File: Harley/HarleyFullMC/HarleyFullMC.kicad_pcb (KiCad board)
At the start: 10 copper layers, 33 x 45 mm, 209 parts, among them J1 USB_3.1_microB, J3 CONN_01X04, J4 CONN_02X05, J5 DF40C_60DP_0-4V, J6 CONN_01X06, U1 xc7a50tcsg324pkg, U10 LTM4622, U11 OSCILLATOR, U12 24LC128T-I/MNY, U2 LTM4622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

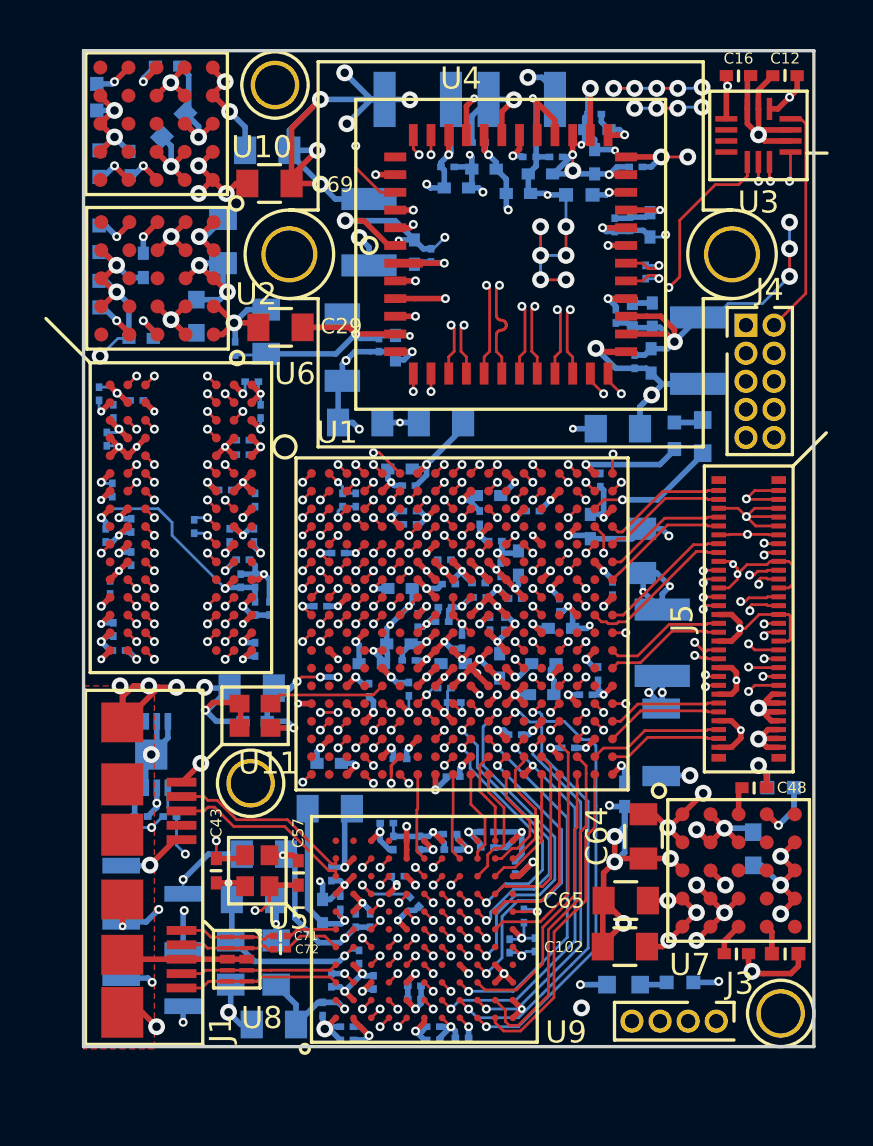
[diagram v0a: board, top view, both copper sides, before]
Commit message: fixed things based on Harley Notes, not ready for fab yet
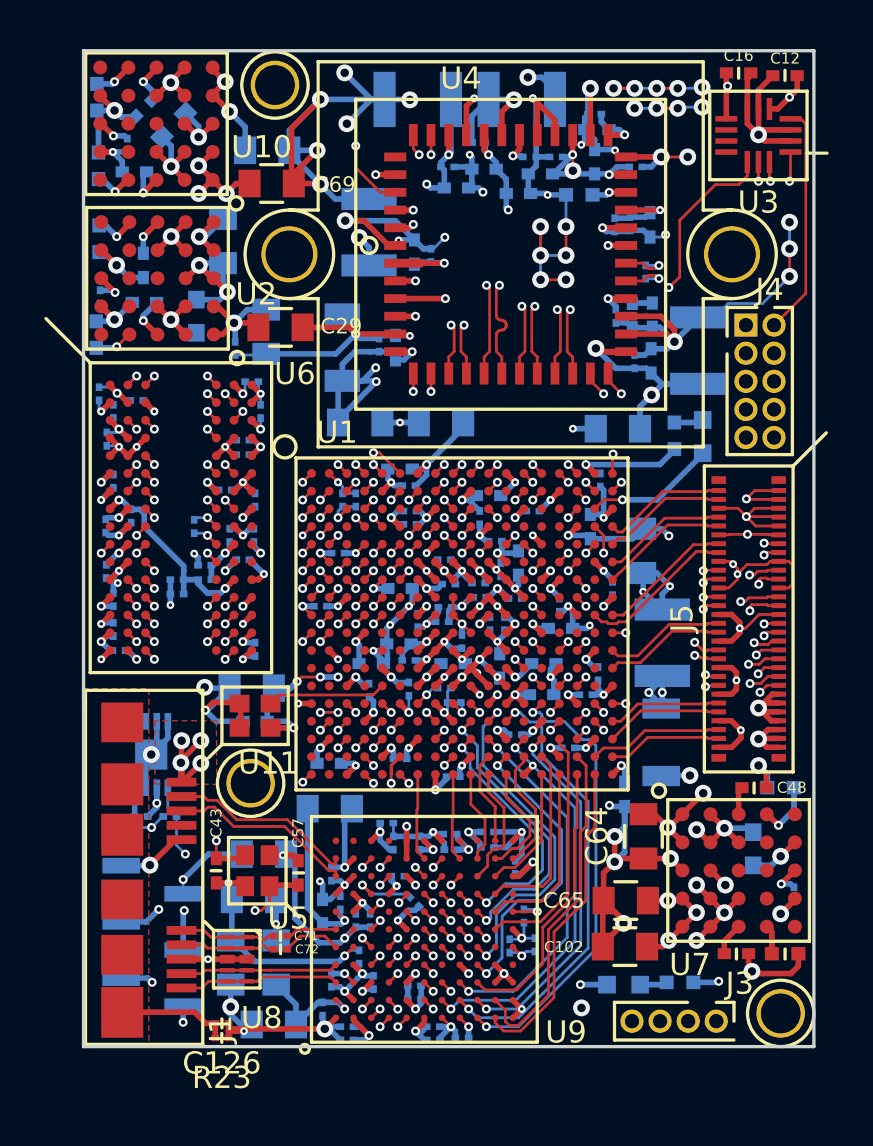
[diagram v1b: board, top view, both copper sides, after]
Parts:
- added C126: 4.7n, Dipoles_SMD:C_0201, F.Cu at (18.2, 196.9)
- added R23: 1M, Dipoles_SMD:C_0201, F.Cu at (18.2, 197.6)
- added R24: R, Dipoles_SMD:C_0201, B.Cu at (44.1, 191.1)
- added R25: R, Dipoles_SMD:C_0201, B.Cu at (12.8, 164.1)
- added R26: R, Dipoles_SMD:C_0201, B.Cu at (14.0, 157.3)
- moved R7 3.53 mm to (16.2, 176.9), turned to 180 degrees
- moved C49 3.52 mm to (17.5, 176.2), turned to 180 degrees
- moved C26 2.94 mm to (16.2, 177.6), turned to 180 degrees
- moved R6 2.62 mm to (17.5, 176.9), turned to 180 degrees
- moved C66 2.18 mm to (14.7, 155.6), turned to 225 degrees
- moved R8 1.83 mm to (12.6, 165.8)
- moved C3 1.63 mm to (14.8, 164.4)
- moved C23 1.45 mm to (14.2, 174.0)
- moved C45 1.26 mm to (13.0, 176.5)
- moved C60 1.15 mm to (13.0, 174.5)
- moved C50 0.57 mm to (13.3, 177.8)
- moved C68 0.43 mm to (14.3, 158.5), turned to 180 degrees
- moved C51 0.40 mm to (13.3, 172.4)
- moved C16 0.12 mm to (41.6, 154.0)
- moved R5 0.10 mm to (12.7, 158.2)
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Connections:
- J1 pad SHLD: GND -> Net-(C126-Pad1)
- J5 pad 36: GND -> FPGA_SS_CCLK
- J5 pad 38: FPGA_SS_CCLK -> FPGA_SS_DIN
- U10 pad C5: GND -> Net-(R26-Pad1)
- U12 pad EPAD: (no net) -> GND
- U2 pad C5: GND -> Net-(R25-Pad1)
- U7 pad C5: GND -> Net-(R24-Pad1)
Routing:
- net GND: track 405.8 -> 387.6 mm, vias 211 -> 208
- net FPGA_SS_DIN: track 32.6 -> 40.0 mm, vias 2 -> 3
- net +1V8: track 41.7 -> 35.8 mm
- net Net-(C126-Pad1): track 0.00 -> 5.07 mm
- net +5V: track 33.2 -> 38.2 mm, vias 13 -> 16
- net DDR_VREF: track 11.7 -> 9.29 mm
- net Net-(R25-Pad1): track 0.00 -> 1.62 mm, vias 0 -> 1
- net Net-(R24-Pad1): track 0.00 -> 1.50 mm, vias 0 -> 1
- net Net-(R26-Pad1): track 0.00 -> 1.50 mm, vias 0 -> 1
- net DDR_CAS#: track 8.62 -> 9.42 mm
- net (no net): track 0.00 -> 0.80 mm, vias 1 -> 3
- net DDR_RAS#: track 9.29 -> 10.1 mm
- net DDR_VDD: track 47.8 -> 48.5 mm
- net FPGA_SS_CCLK: track 44.7 -> 44.2 mm
- added copper zone on F.Cu, net +5V
- added copper zone on F.Cu, net Net-(C126-Pad1)
- removed copper zone on F.Cu, net GND

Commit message: fixed footprints and rerouted imager
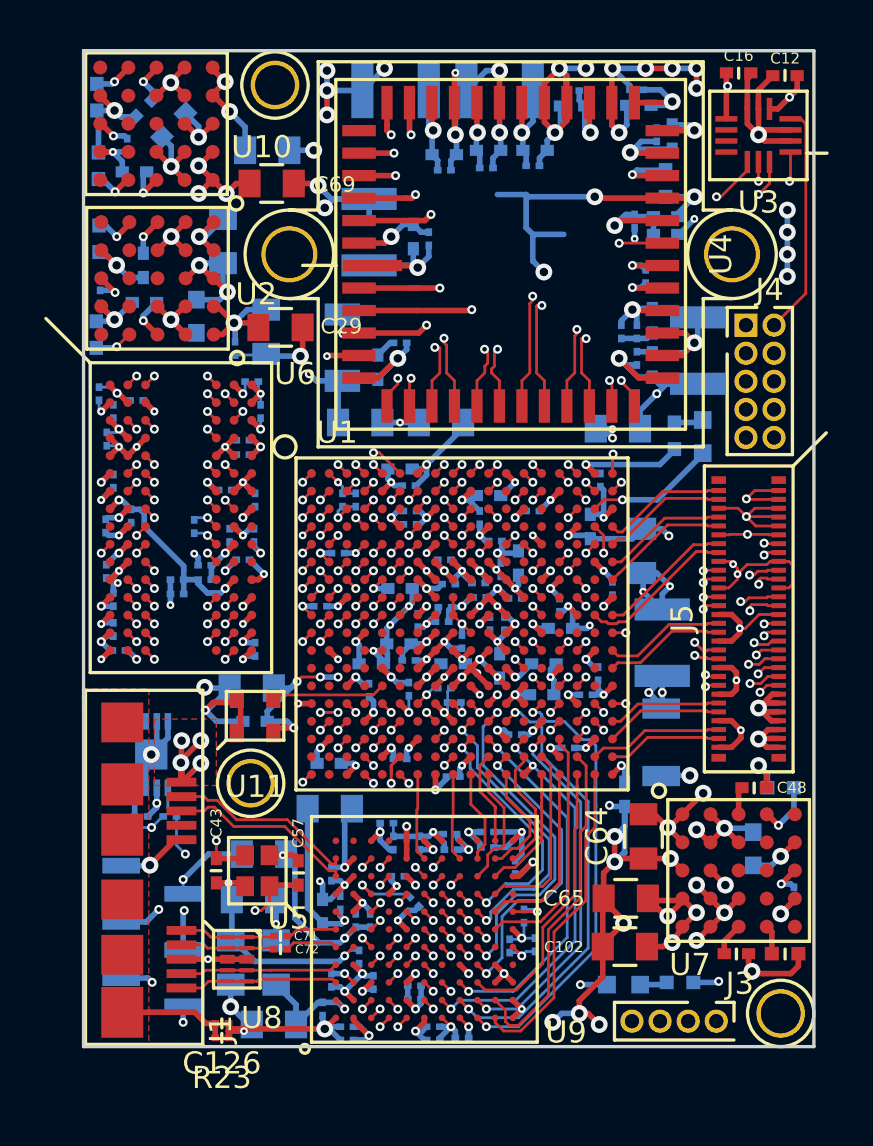
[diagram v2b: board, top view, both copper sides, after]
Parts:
- U11: footprint Oscillator:8y -> Oscillator:ASDMB
- U4: footprint ONSemi:CLCC48_0.8mm -> LCC:LCC101.6P1422X1422X165-48
- moved C27 10.9 mm to (32.4, 157.5), turned to 0 degrees
- moved C34 9.83 mm to (37.7, 167.2), turned to 90 degrees
- moved C21 6.13 mm to (32.3, 158.2), turned to 0 degrees
- moved C13 5.86 mm to (27.6, 161.5), turned to 90 degrees
- moved C6 4.89 mm to (37.0, 165.7), turned to 270 degrees
- moved C11 4.84 mm to (36.3, 165.7), turned to 270 degrees
- moved C30 4.49 mm to (38.3, 160.5), turned to 0 degrees
- moved C15 4.38 mm to (36.9, 160.7)
- moved C19 4.33 mm to (37.7, 165.2), turned to 270 degrees
- moved C22 3.96 mm to (38.3, 161.3), turned to 0 degrees
- moved R4 3.93 mm to (38.3, 159.0), turned to 270 degrees
- moved C39 3.68 mm to (38.6, 156.9)
- moved C8 3.40 mm to (34.1, 155.5)
- moved C28 3.09 mm to (34.1, 154.8)
- moved C36 2.20 mm to (37.0, 154.8)
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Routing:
- net GND: track 387.6 -> 367.4 mm, vias 208 -> 201
- net P_LVDS4+: track 7.17 -> 14.0 mm
- net P_LVDS4-: track 7.11 -> 13.9 mm
- net P_LVDS8-: track 6.64 -> 12.9 mm
- net P_LVDS8+: track 7.73 -> 14.0 mm
- net P_LVDS7-: track 6.88 -> 13.2 mm
- net P_LVDS7+: track 7.76 -> 14.0 mm
- net CAM_monitor1: track 25.6 -> 20.3 mm
- net FPGA_SS_CCLK: track 44.2 -> 48.5 mm
- net P_LVDS11-: track 9.82 -> 13.9 mm
- net P_LVDS11+: track 9.95 -> 14.0 mm
- net P_LVDS5-: track 9.67 -> 13.7 mm
- net P_LVDS5+: track 9.99 -> 14.0 mm
- net SPI_MOSI: track 31.3 -> 35.1 mm
- net CAM_RST#: track 14.6 -> 17.7 mm
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
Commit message: switched to lever 3 stack, changed USB shielding capacitor, cleaned some traces
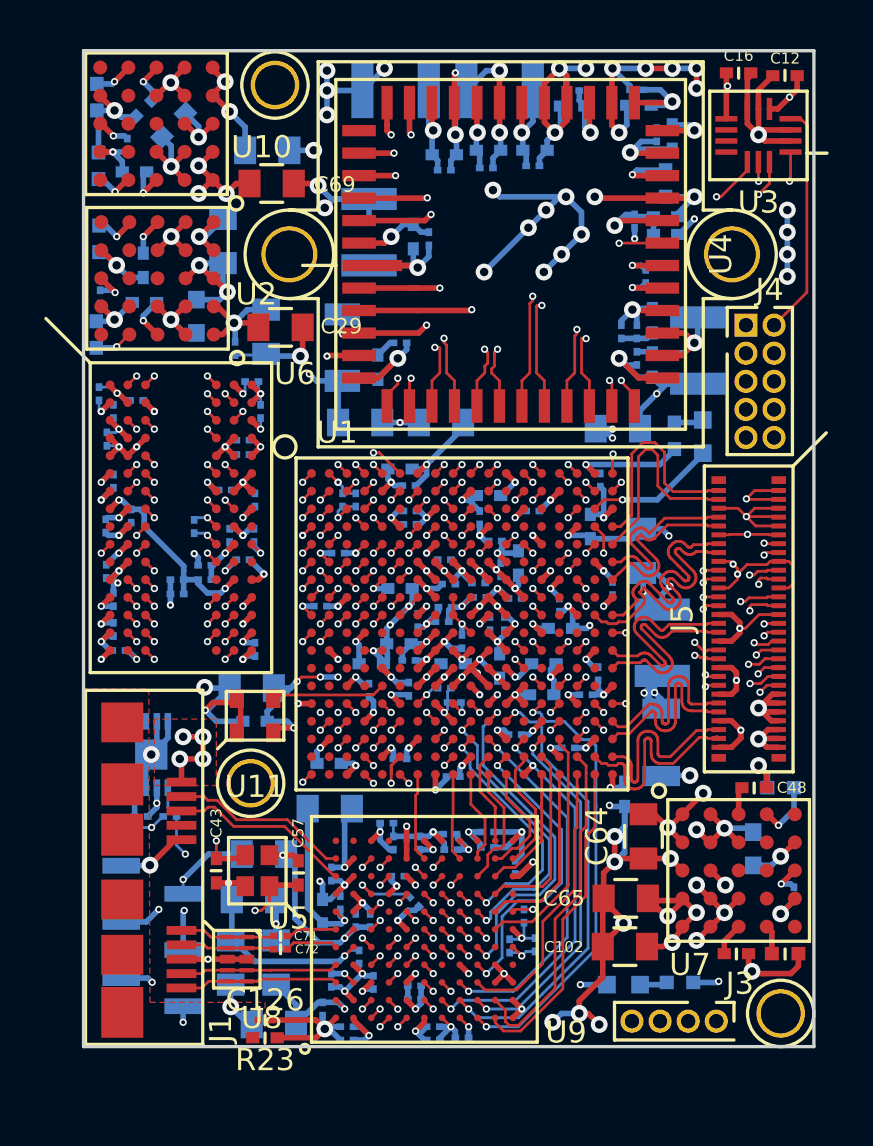
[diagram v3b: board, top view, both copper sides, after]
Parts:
- C126: footprint Dipoles_SMD:C_0201 -> Dipoles_SMD:C_0402
- moved R23 2.11 mm to (20.2, 196.8)
- moved C126 2.06 mm to (20.2, 197.6)
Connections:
- U1 pad U17: P_LVDS10- -> P_LVDS10+
- U1 pad U18: P_LVDS10+ -> P_LVDS10-
- U12 pad EPAD: GND -> (no net)
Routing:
- net GND: track 367.4 -> 353.1 mm, vias 201 -> 199
- net +3V3: track 65.7 -> 52.8 mm
- net (no net): track 3.80 -> 15.9 mm, vias 6 -> 14
- net +1V2: track 35.1 -> 23.7 mm
- net +1V0: track 36.3 -> 25.0 mm
- net +2V5: track 82.4 -> 73.1 mm
- net DDR_VDD: track 48.5 -> 41.9 mm
- net P_LVDS3+: track 7.13 -> 12.5 mm
- net P_LVDS3-: track 6.14 -> 11.5 mm
- net P_LVDS10+: track 5.18 -> 10.3 mm
- net Net-(C126-Pad1): track 5.07 -> 0.00 mm
- net P_LVDS1+: track 5.68 -> 9.96 mm
- net P_LVDS1-: track 5.68 -> 9.75 mm
- net P_LVDS6+: track 5.51 -> 9.43 mm
- net P_LVDS6-: track 5.51 -> 9.43 mm
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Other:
- net class Default: via_dia 0.4064 -> 0.3302; via_drill 0.2032 -> 0.1778
- rule via_min_drill: 0.2032 -> 0.1778
- rule via_min_size: 0.4 -> 0.3302

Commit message: backup before attempting to solve Mask/Paste issue
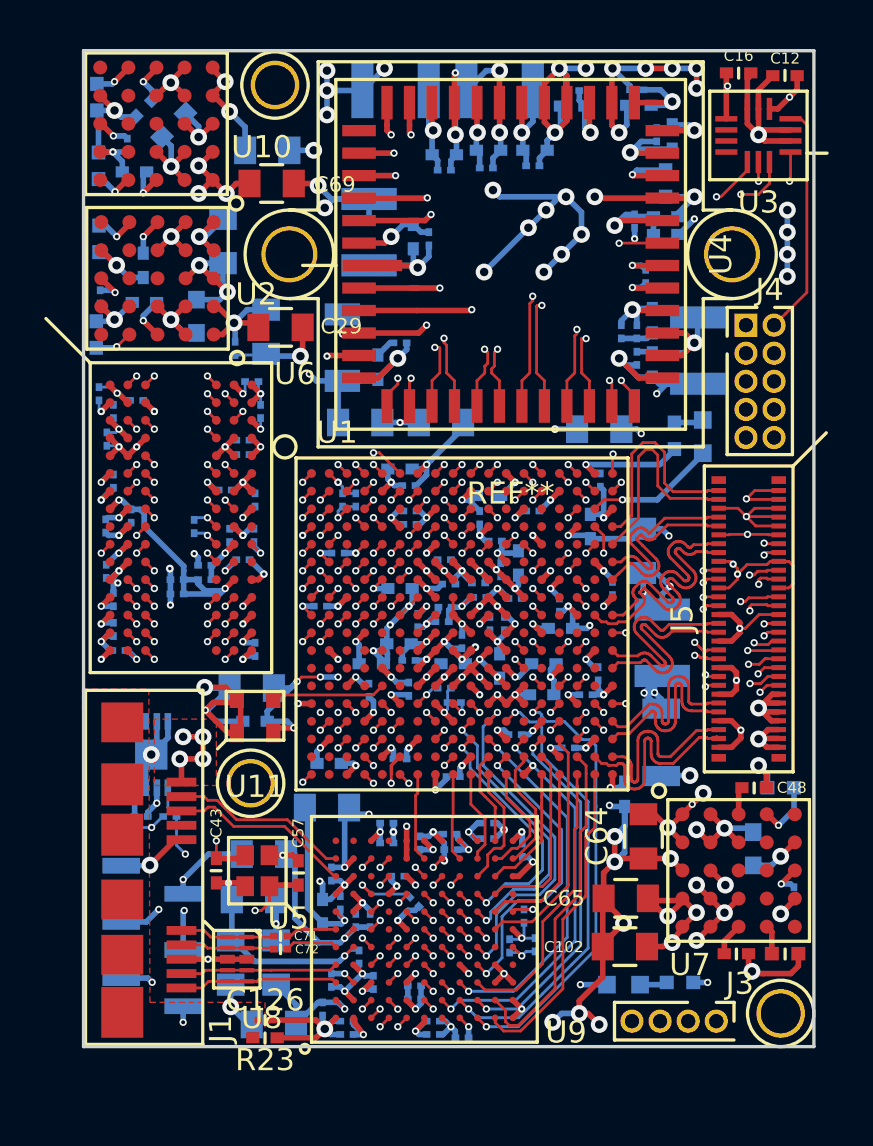
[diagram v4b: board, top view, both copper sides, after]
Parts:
- moved C108 0.84 mm to (35.3, 170.1)
- moved C88 0.84 mm to (31.8, 189.1)
- moved C78 0.40 mm to (30.2, 188.6)
- moved C95 0.40 mm to (30.2, 187.9)
- moved G*** 0.35 mm to (42.8, 178.8)
- moved C85 0.30 mm to (25.7, 188.8), turned to 0 degrees
- moved C77 0.25 mm to (27.8, 197.4)
- moved C83 0.25 mm to (23.9, 196.8)
- moved C94 0.25 mm to (27.8, 196.8)
- moved C99 0.25 mm to (23.9, 197.4)
- moved G*** 0.20 mm to (42.1, 157.4)
- moved FB3 0.13 mm to (23.0, 187.2)
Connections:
- U12 pad EPAD: (no net) -> GND
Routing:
- net GND: track 353.1 -> 350.3 mm, vias 199 -> 202
- net +2V5: track 73.1 -> 75.0 mm, vias 35 -> 36
- net FX3_FLAGA: track 10.4 -> 8.45 mm
- net DDR_VREF: track 9.29 -> 11.1 mm
- net FX3_PKT_END#: track 12.0 -> 11.0 mm
- net FX3_DQ4: track 9.75 -> 8.78 mm
- net +3V3: track 52.8 -> 51.9 mm, vias 14 -> 15
- net FPGA_SS_DONE: track 33.6 -> 34.3 mm
- net FX3_DQ5: track 10.9 -> 10.2 mm
- net FX3_DQ15: track 10.2 -> 9.58 mm
- net +1V2: track 23.7 -> 24.2 mm, vias 12 -> 13
- net FX3_SLRD#: track 12.0 -> 11.5 mm
- net +1V0: vias 12 -> 13
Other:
- board text added: "GND RST RX TX"

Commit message: placed conmponent references on Silkscreen
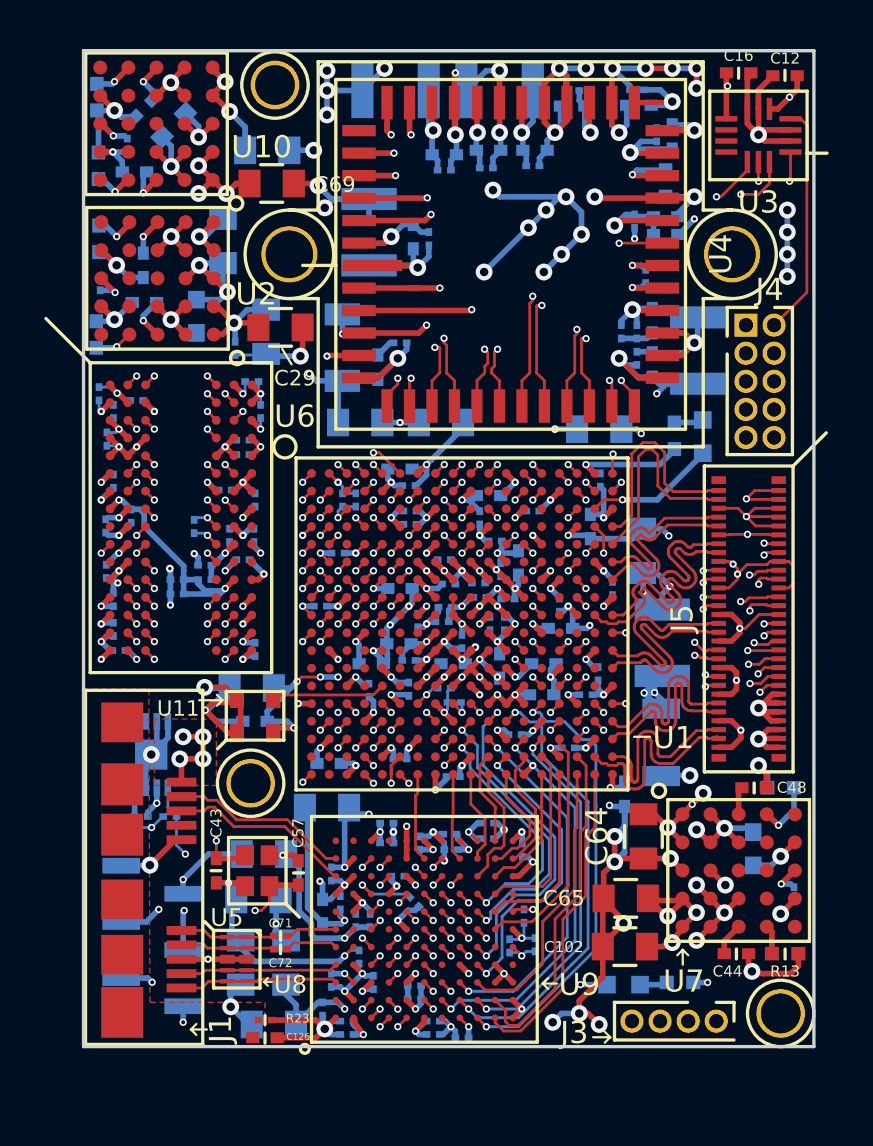
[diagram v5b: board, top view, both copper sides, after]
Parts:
- moved FB1 0.45 mm to (19.1, 194.2)
- moved C82 0.45 mm to (21.1, 194.2)
- moved C119 0.33 mm to (31.2, 177.8)
- moved C74 0.20 mm to (19.9, 191.3)

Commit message: updated Silkscreen and added 3d models
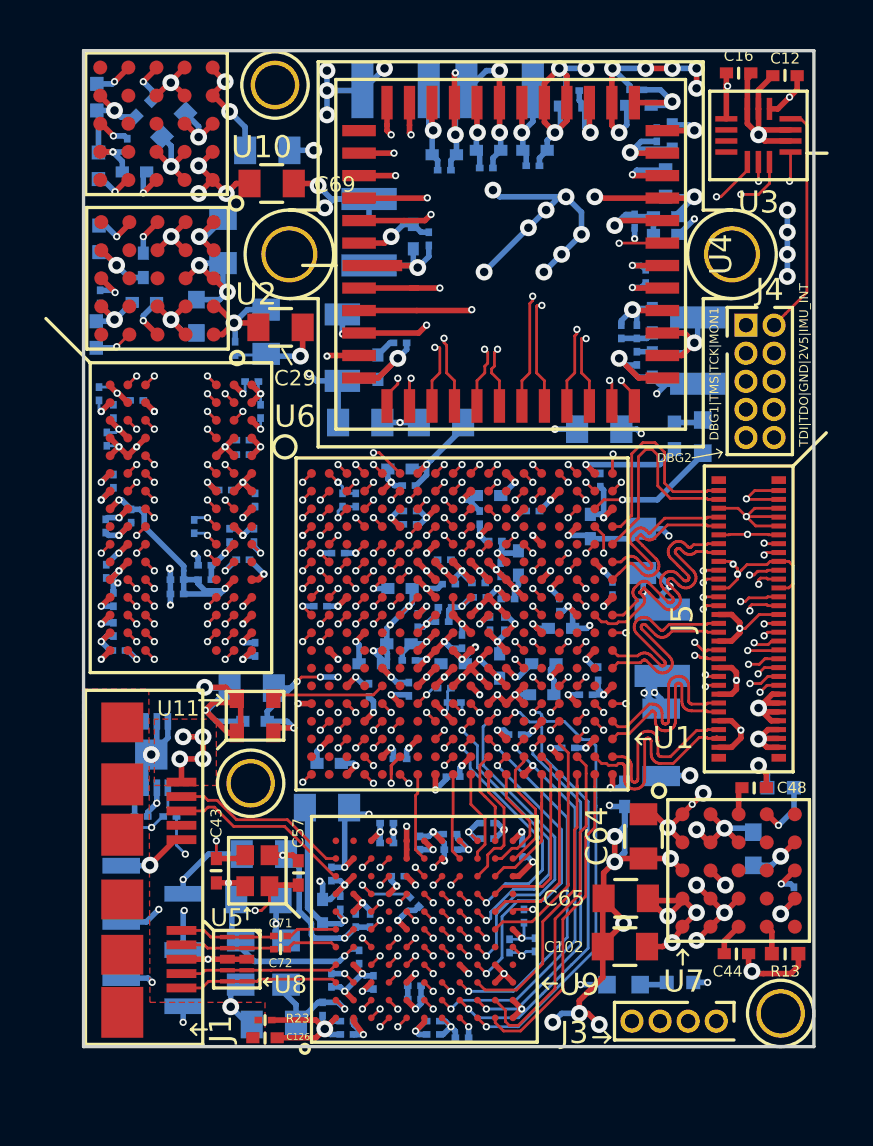
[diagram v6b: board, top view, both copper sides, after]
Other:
- board text added: "2V5"
- board text added: "DBG1|TMS|TCK|MON1"
- board text added: "DBG2"
- board text added: "GND"
- board text added: "GND|RST|RX|TX"
- board text added: "IMU_INT"
- board text added: "TDI|TDO|GND|2V5|IMU_INT"
- board text removed: "GND RST RX TX"
